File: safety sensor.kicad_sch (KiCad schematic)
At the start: 10 parts

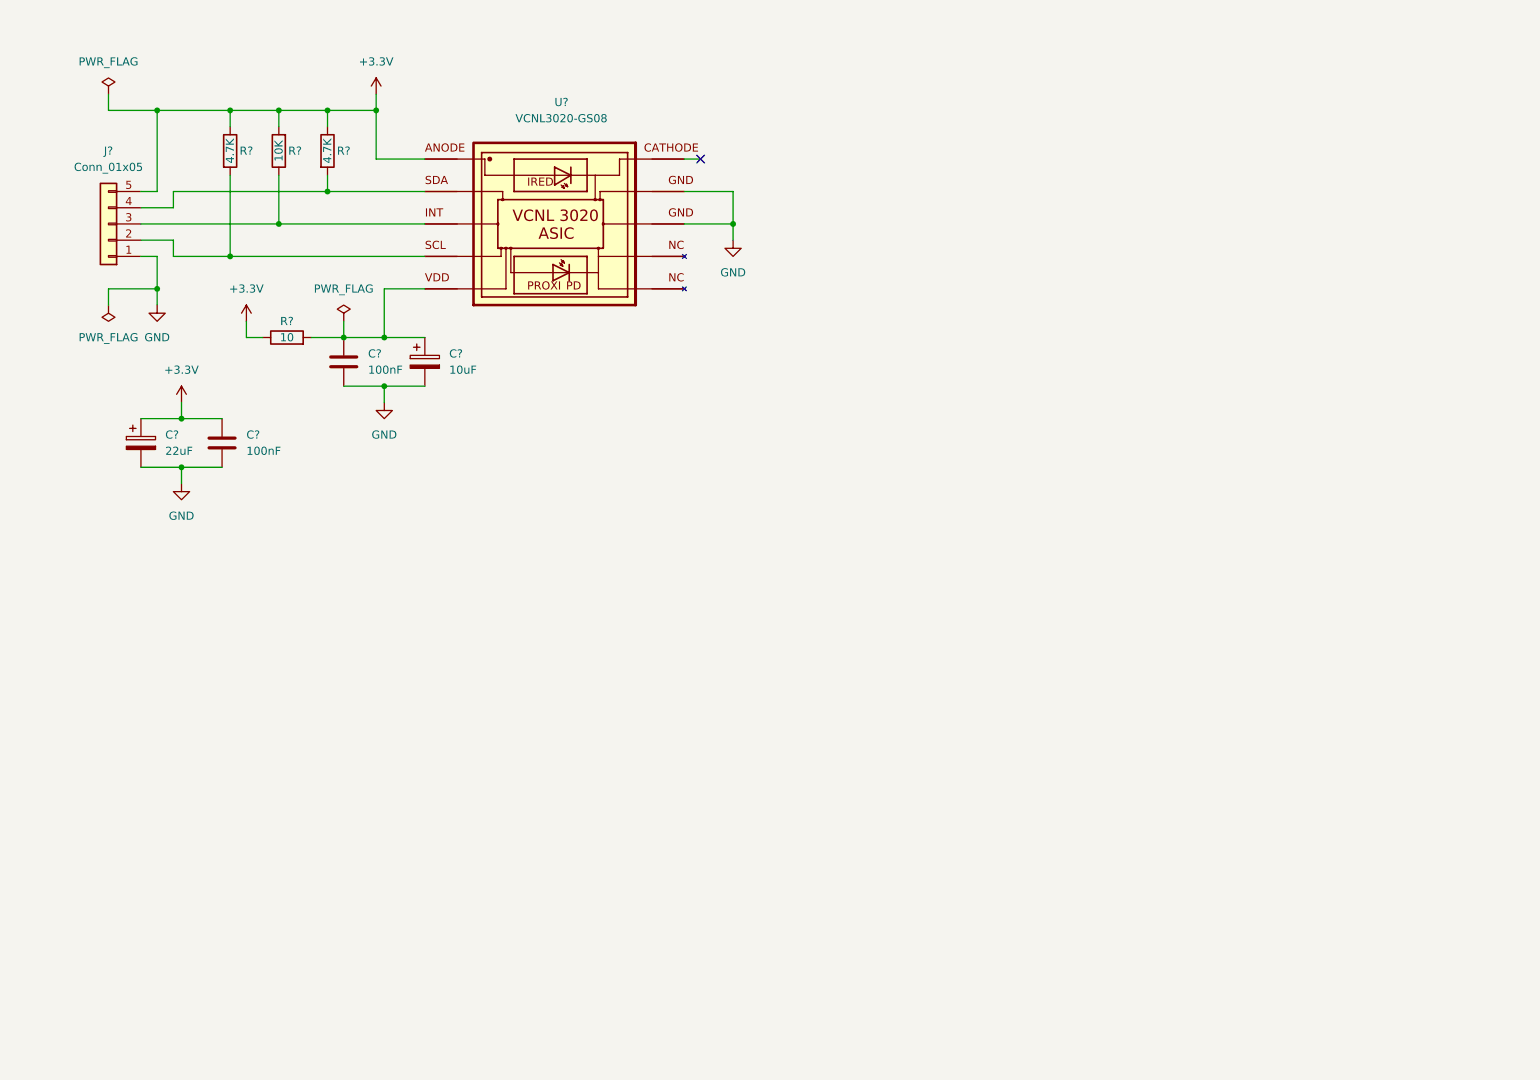
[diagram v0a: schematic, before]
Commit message: add stm8 to the board with connection to interrupt line of vcnl3020
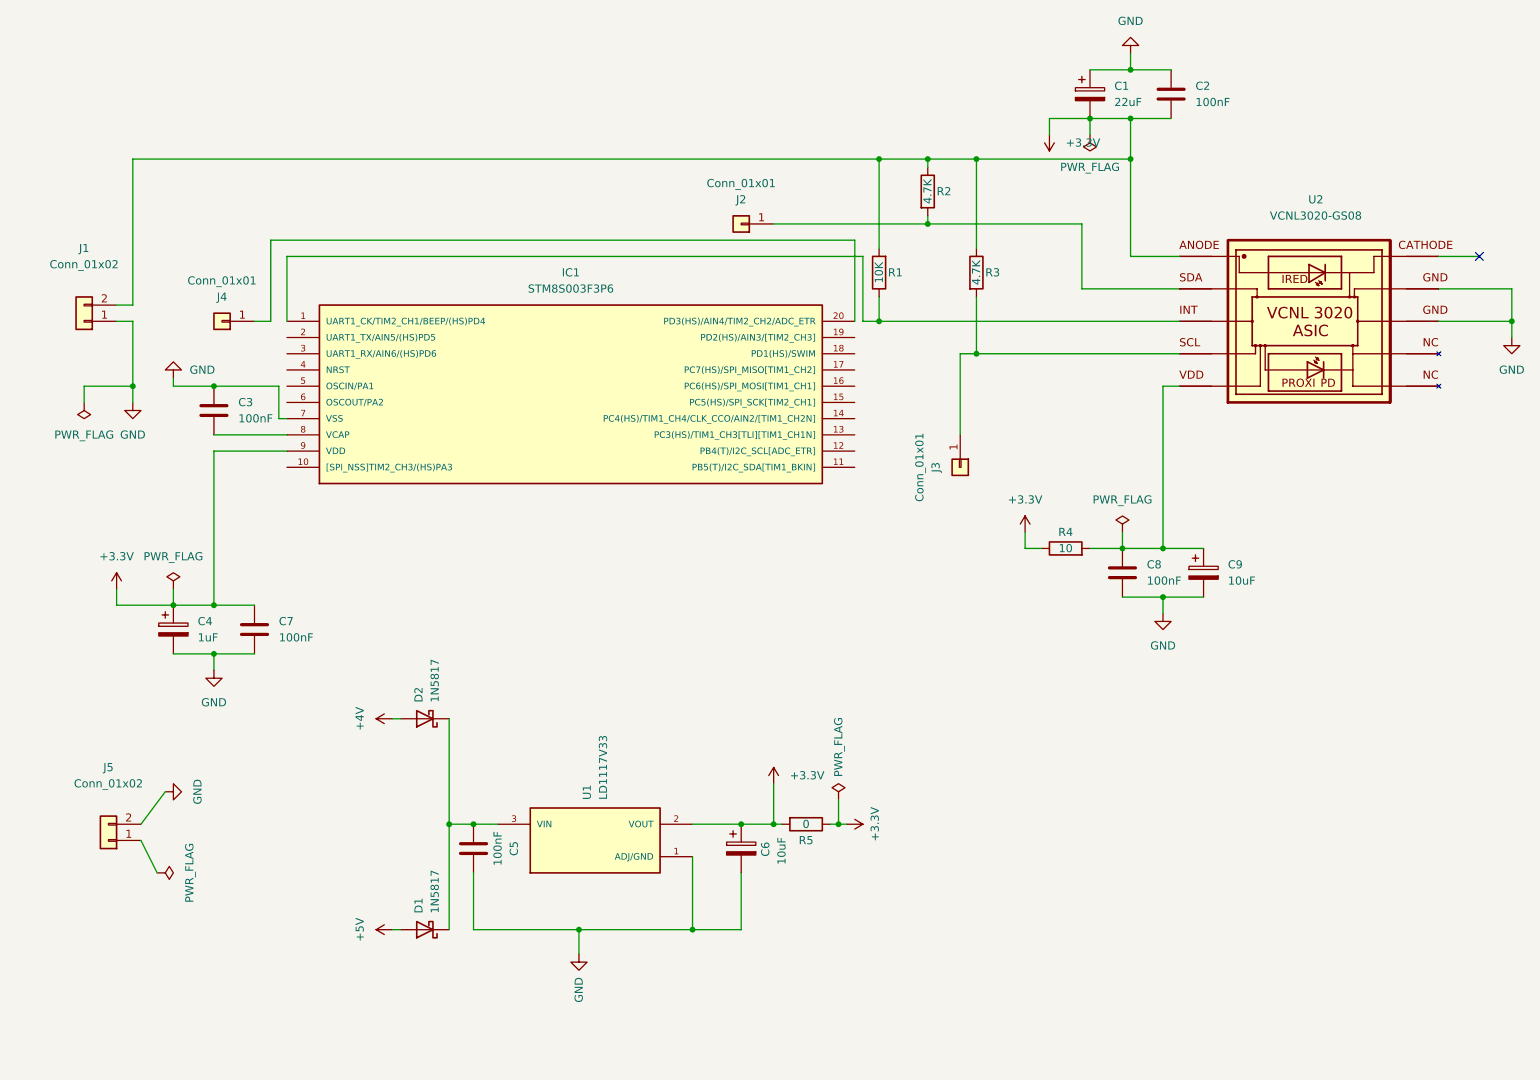
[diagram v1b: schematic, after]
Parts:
- removed C?: 22uF, Capacitor_THT:CP_Radial_D4.0mm_P2.00mm, symbol Device:C_Polarized
- removed C?: 100nF, Capacitor_THT:C_Disc_D3.0mm_W2.0mm_P2.50mm, symbol Device:C
- removed R? (x2): 4.7K, Resistor_THT:R_Axial_DIN0207_L6.3mm_D2.5mm_P10.16mm_Horizontal, symbol Device:R
- removed R?: 10K, Resistor_THT:R_Axial_DIN0207_L6.3mm_D2.5mm_P10.16mm_Horizontal, symbol Device:R
- added C1: 22uF, Capacitor_THT:CP_Radial_D4.0mm_P2.00mm, symbol Device:C_Polarized
- added C2, C3, C5, C7: 100nF, Capacitor_THT:C_Disc_D3.0mm_W2.0mm_P2.50mm, symbol Device:C
- added C4: 1uF, Capacitor_THT:CP_Radial_D4.0mm_P2.00mm, symbol Device:C_Polarized
- added C6: 10uF, Capacitor_THT:CP_Radial_D4.0mm_P2.00mm, symbol Device:C_Polarized
- added D1, D2: 1N5817, Diode_THT:D_DO-41_SOD81_P10.16mm_Horizontal, symbol Diode:1N5817
- added IC1: STM8S003F3P6, safety sensor:TSSOP20, symbol STM8S003F3P6:STM8S003F3P6
- added J2, J3, J4: Conn_01x01, Connector_PinHeader_2.54mm:PinHeader_1x01_P2.54mm_Vertical, symbol Connector_Generic:Conn_01x01
- added J5: Conn_01x02, Connector_PinHeader_2.54mm:PinHeader_1x02_P2.54mm_Vertical, symbol Connector_Generic:Conn_01x02
- added R1: 10K, Resistor_THT:R_Axial_DIN0207_L6.3mm_D2.5mm_P10.16mm_Horizontal, symbol Device:R
- added R2, R3: 4.7K, Resistor_THT:R_Axial_DIN0207_L6.3mm_D2.5mm_P10.16mm_Horizontal, symbol Device:R
- added R5: 0, Resistor_THT:R_Axial_DIN0207_L6.3mm_D2.5mm_P15.24mm_Horizontal, symbol Device:R
- added U1: LD1117V33, safety sensor:TO255P1020X450X1968-3, symbol LD1117V33:LD1117V33
- J1: renamed from J?; value Conn_01x05 -> Conn_01x02; footprint Connector_PinHeader_2.54mm:PinHeader_1x05_P2.54mm_Vertical -> Connector_PinHeader_2.54mm:PinHeader_1x02_P2.54mm_Vertical; symbol Connector_Generic:Conn_01x05 -> Connector_Generic:Conn_01x02
- U2: renamed from U?; footprint XDCR_VCNL3020-GS08 -> safety sensor:XDCR_VCNL3020-GS08
- gave numbers to parts that had none: 3
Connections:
- net +3.3V: now also J1.2 (Pin_2), C1.2, C2.2, C4.1, C6.1, C7.1, IC1.9 (VDD), R1.2, R2.1, R3.1, R5.1, R5.2, U1.2 (VOUT); no longer J1.5 (Pin_5)
- net GND: now also C1.1, C2.1, C3.1, C4.2, C5.1, C6.2, C7.2, IC1.7 (VSS), J5.2 (Pin_2), U1.1 (ADJ/GND)
- net at U2.4: now also J3.1 (Pin_1), R3.2; no longer J1.2 (Pin_2)
- net at U2.3: now also IC1.1 (UART1_CK/TIM2_CH1/BEEP/(HS)PD4), R1.1; no longer J1.3 (Pin_3)
- net at U2.2: now also J2.1 (Pin_1), R2.2; no longer J1.4 (Pin_4)
- new net: IC1.20 (PD3(HS)/AIN4/TIM2_CH2/ADC_ETR), J4.1 (Pin_1)
- new net: C5.2, D1.1 (K), D2.1 (K), U1.3 (VIN)
- new net: C3.2, IC1.8 (VCAP)
- new net +4V: D2.2 (A)
- new net +5V: D1.2 (A)
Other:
- moved on the sheet: C8, C9, R4, U2

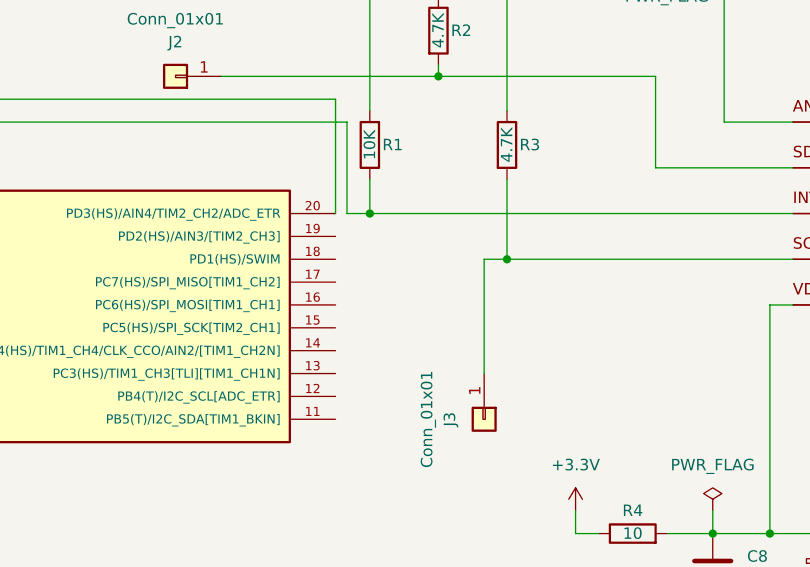
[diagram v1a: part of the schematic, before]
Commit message: add SWIM connector
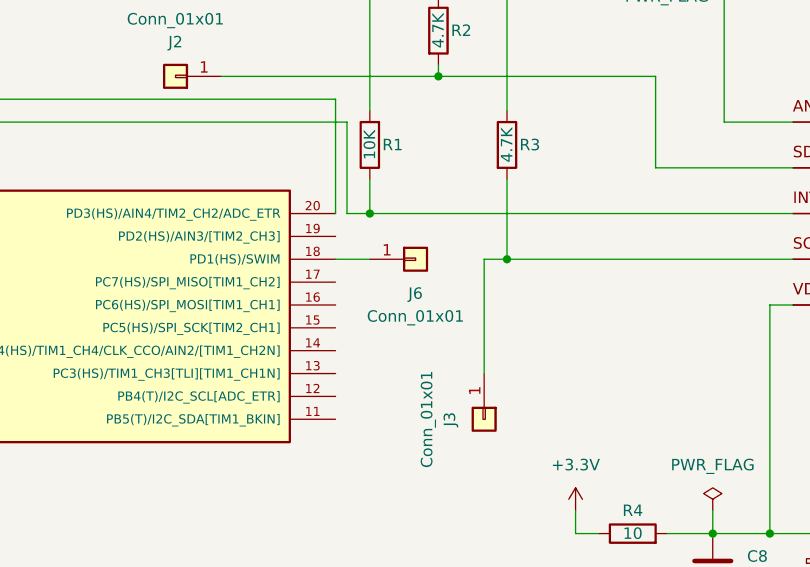
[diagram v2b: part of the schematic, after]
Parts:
- added J6: Conn_01x01, Connector_PinHeader_2.54mm:PinHeader_1x01_P2.54mm_Vertical, symbol Connector_Generic:Conn_01x01
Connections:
- net at IC1.18 (PD1(HS)/SWIM): now also J6.1 (Pin_1)
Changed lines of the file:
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@@
+    (stroke (width 0) (type default) (color 0 0 0 0))
+  )
+  (wire (pts (xy 149.86 67.31) (xy 153.67 67.31))
     (stroke (width 0) (type default) (color 0 0 0 0))
   )
@@
     (pin "1")
   )
+  (symbol (lib_id "Connector_Generic:Conn_01x01") (at 158.75 67.31 0) (unit 1)
+    (in_bom yes) (on_board yes)
+    (property "Reference" "J6" (id 0) (at 158.75 71.12 0))
+    (property "Value" "Conn_01x01" (id 1) (at 158.75 73.66 0))
+    (property "Footprint" "Connector_PinHeader_2.54mm:PinHeader_1x01_P2.54mm_Vertical" (id 2) (at 158.75 67.31 0)
+      (effects (font (size 1.27 1.27)) hide)
+    )
+    (property "Datasheet" "~" (id 3) (at 158.75 67.31 0)
+      (effects (font (size 1.27 1.27)) hide)
+    )
+    (pin "1")
+  )
   (symbol (lib_id "Device:C") (at 49.53 76.2 0) (unit 1)
     (in_bom yes) (on_board yes) (fields_autoplaced)
@@
       (reference "J5") (unit 1) (value "Conn_01x02") (footprint "Connector_PinHeader_2.54mm:PinHeader_1x02_P2.54mm_Vertical")
     )
+    (path "/880751c1-2174-42b0-a015-b89b331b6e99"
+      (reference "J6") (unit 1) (value "Conn_01x01") (footprint "Connector_PinHeader_2.54mm:PinHeader_1x01_P2.54mm_Vertical")
+    )
     (path "/5f77b1fe-0a0b-49db-825a-edda5840d9b2"

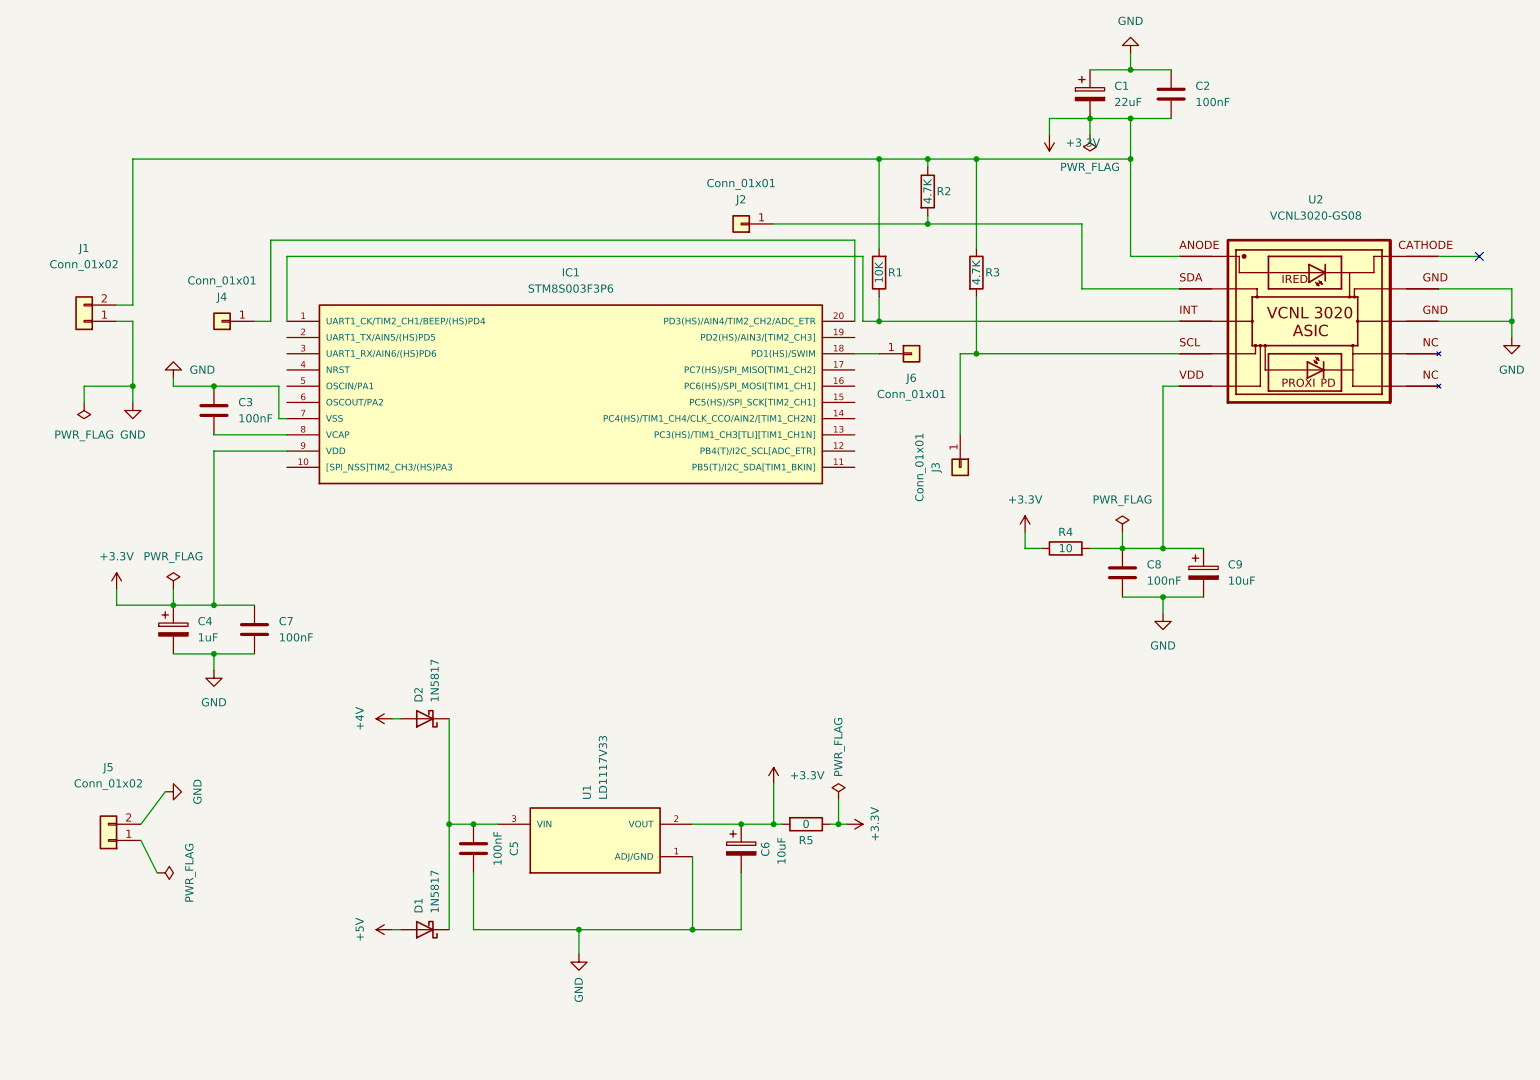
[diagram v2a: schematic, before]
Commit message: polish schematics, add leds for voltage lines and gpio for stm8
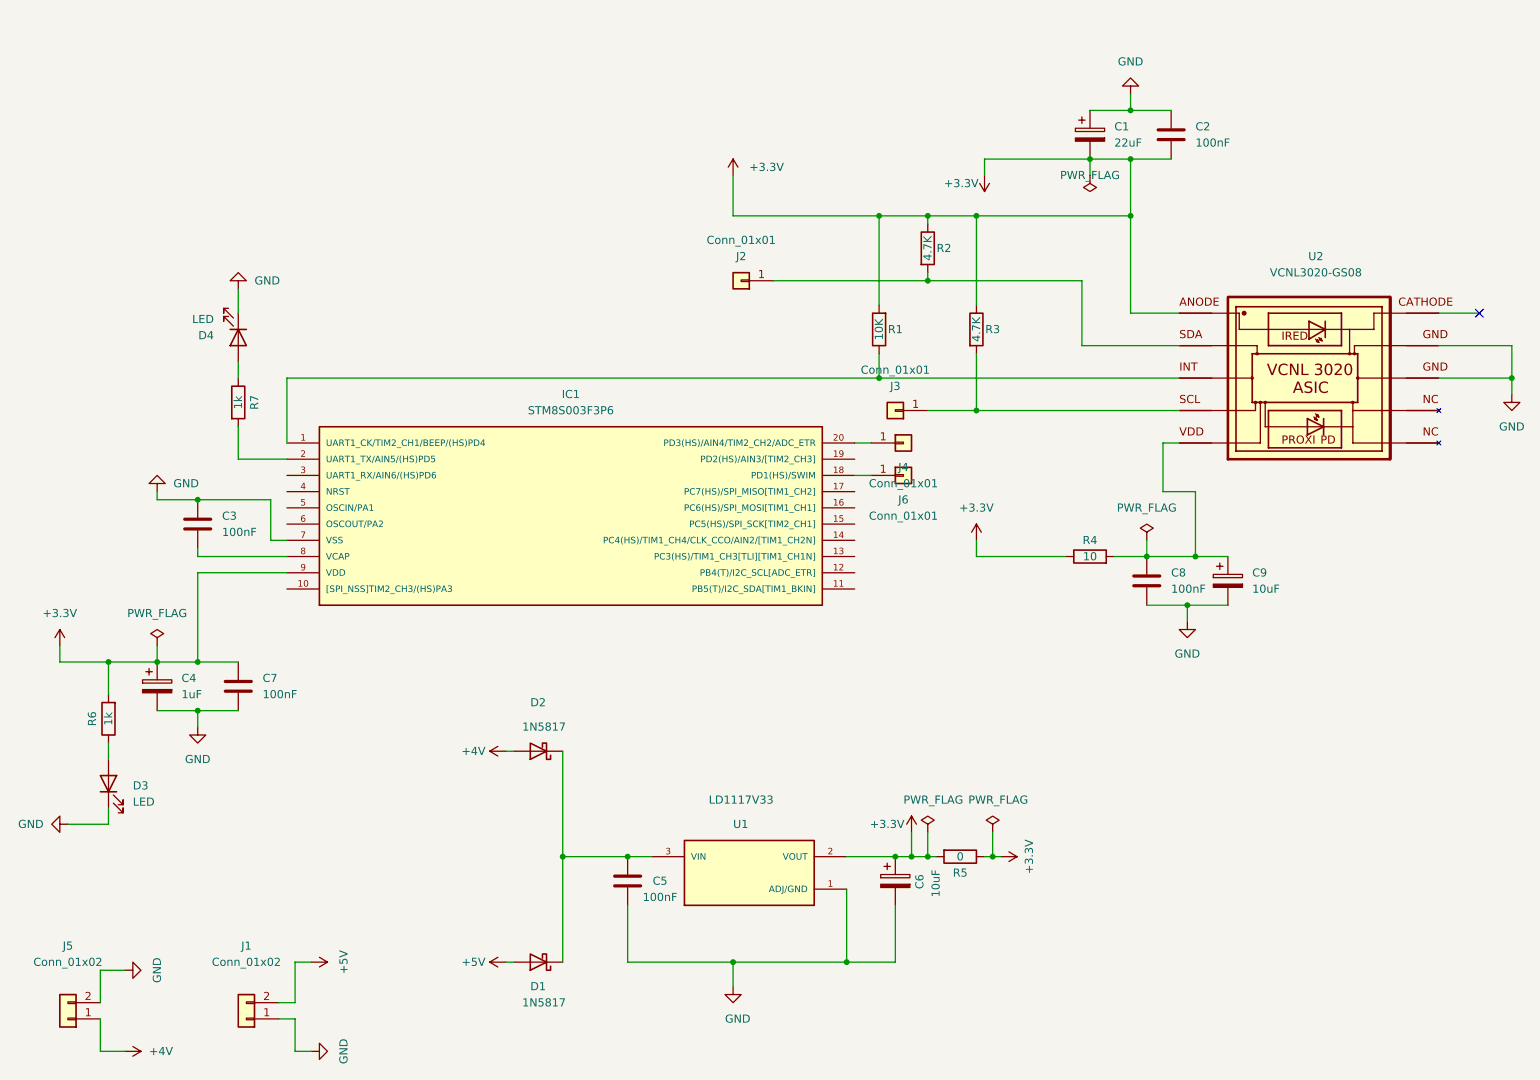
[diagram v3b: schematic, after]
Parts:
- added D3, D4: LED, LED_THT:LED_D5.0mm, symbol Device:LED
- added R6, R7: 1k, Resistor_THT:R_Axial_DIN0207_L6.3mm_D2.5mm_P10.16mm_Horizontal, symbol Device:R
- C1, C4, C6, C9: footprint Capacitor_THT:CP_Radial_D4.0mm_P2.00mm -> Capacitor_THT:CP_Radial_D5.0mm_P2.50mm
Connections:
- net +3.3V: now also R6.2; no longer J1.2 (Pin_2)
- net +4V: now also J5.1 (Pin_1)
- net +5V: now also J1.2 (Pin_2)
- net GND: now also D3.1 (K), D4.1 (K)
- net at IC1.2 (UART1_TX/AIN5/(HS)PD5): now also R7.2
- new net: D4.2 (A), R7.1
- new net: D3.2 (A), R6.1
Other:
- moved on the sheet: C1, C2, C3, C4, C5, C6, C7, C8, C9, D1, D2, IC1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

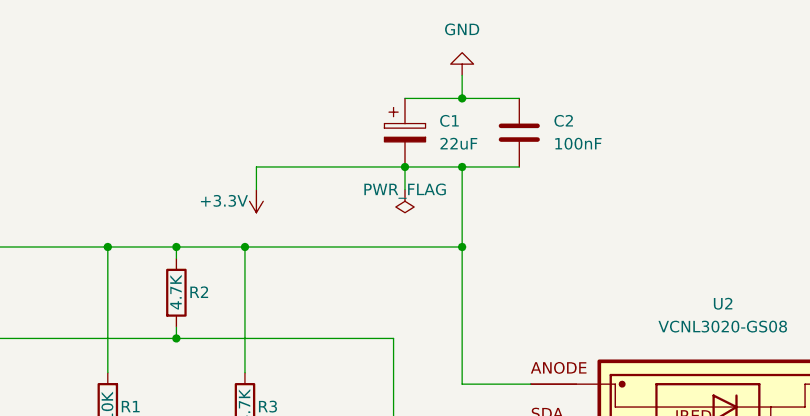
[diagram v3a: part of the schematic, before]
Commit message: fix c1 polarity, fix the hole sizes
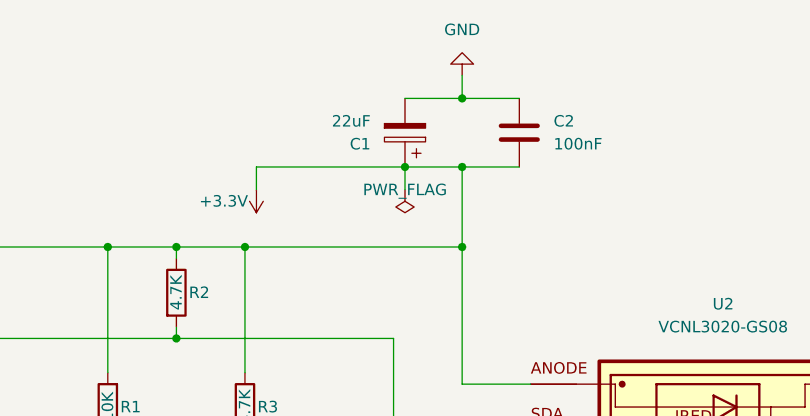
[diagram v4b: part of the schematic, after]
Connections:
- net +3.3V: now also C1.1; no longer C1.2
- net GND: now also C1.2; no longer C1.1
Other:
- moved on the sheet: C1
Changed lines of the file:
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@@
     (pin "2")
   )
-  (symbol (lib_id "Device:C_Polarized") (at 186.69 33.02 0) (unit 1)
+  (symbol (lib_id "Device:C_Polarized") (at 186.69 33.02 180) (unit 1)
     (in_bom yes) (on_board yes)
-    (property "Reference" "C1" (id 0) (at 190.5 31.75 0)
+    (property "Reference" "C1" (id 0) (at 182.88 34.29 0)
       (effects (font (size 1.27 1.27)) (justify left))
     )
-    (property "Value" "22uF" (id 1) (at 190.5 34.29 0)
+    (property "Value" "22uF" (id 1) (at 182.88 31.75 0)
       (effects (font (size 1.27 1.27)) (justify left))
     )
-    (property "Footprint" "Capacitor_THT:CP_Radial_D5.0mm_P2.50mm" (id 2) (at 187.6552 36.83 0)
+    (property "Footprint" "Capacitor_THT:CP_Radial_D5.0mm_P2.50mm" (id 2) (at 185.7248 29.21 0)
       (effects (font (size 1.27 1.27)) hide)
     )
